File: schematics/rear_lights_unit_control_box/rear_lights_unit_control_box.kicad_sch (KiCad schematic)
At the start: 7 parts, among them J1 Conn_01x04_Pin, SW1 SW_SPDT, SW2 SW_SPDT

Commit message: more schematic updates
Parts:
- removed J1: Conn_01x04_Pin, symbol Connector:Conn_01x04_Pin
- added C1, C2: 0.1uF, symbol Device:C
- added C3: 10uF, symbol Device:C_Polarized
- added J1: Conn_01x04_Socket, symbol Connector:Conn_01x04_Socket
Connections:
- net GND: now also C1.1, C2.1, C3.2, J1.4 (Pin_4)
- net LEFT_TURN_EN: now also J1.2 (Pin_2)
- net RIGHT_TURN_EN: now also J1.1 (Pin_1)
- net V_BATT: now also C1.2, C2.2, C3.1, J1.3 (Pin_3)
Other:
- note added: "keep bypass caps as close as possible to inputs"
- note added: "right angle JST"
- note removed: "JST connector (female, right-angle)"
- moved on the sheet: D1, D2, R1, R2, SW1, SW2

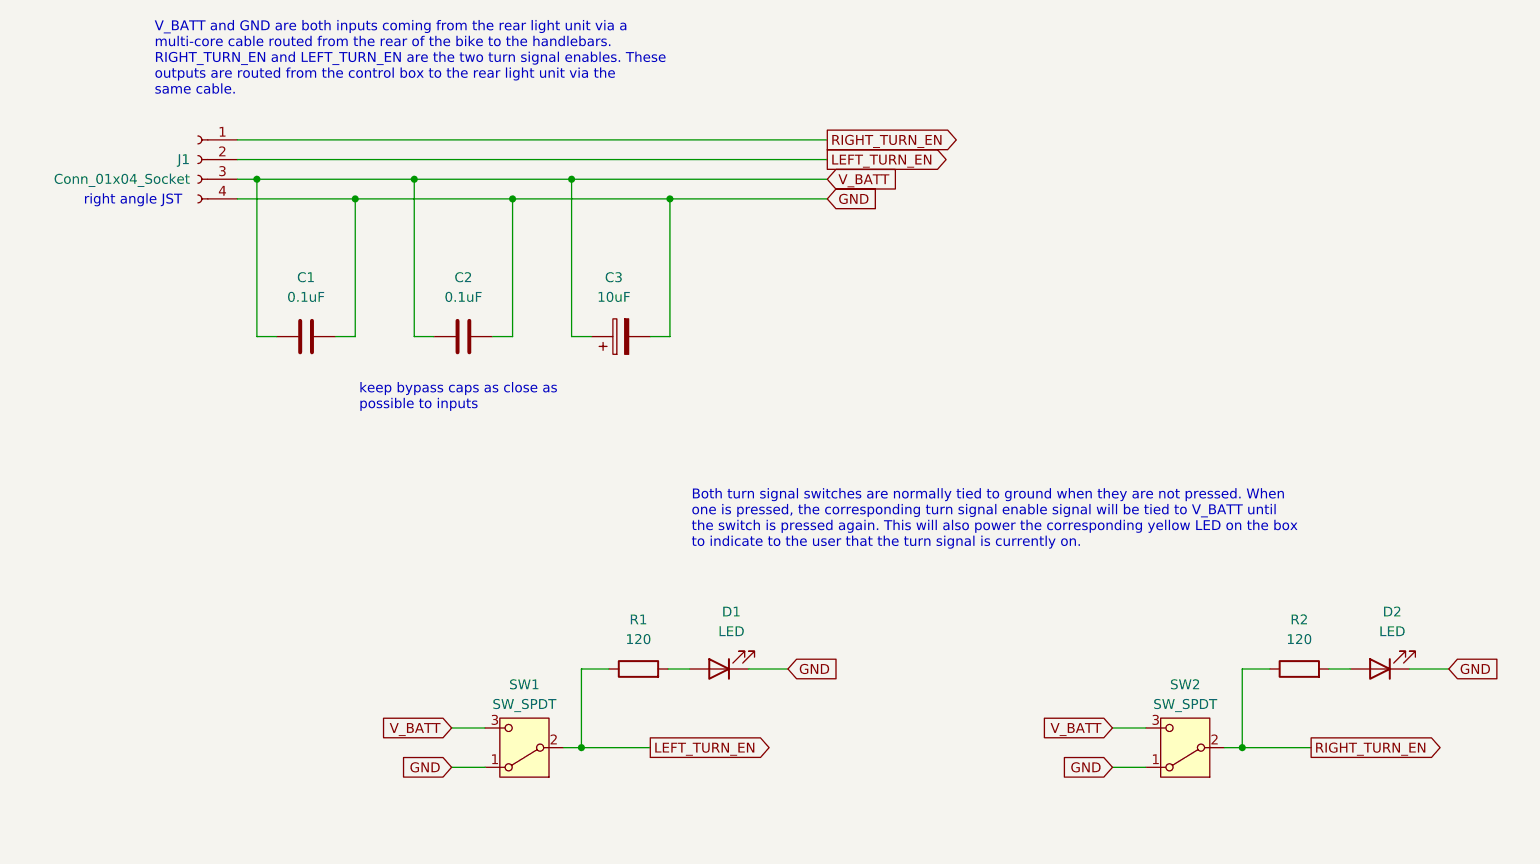
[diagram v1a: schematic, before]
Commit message: finalized rear light unit control box schematic, added corresponding BOM
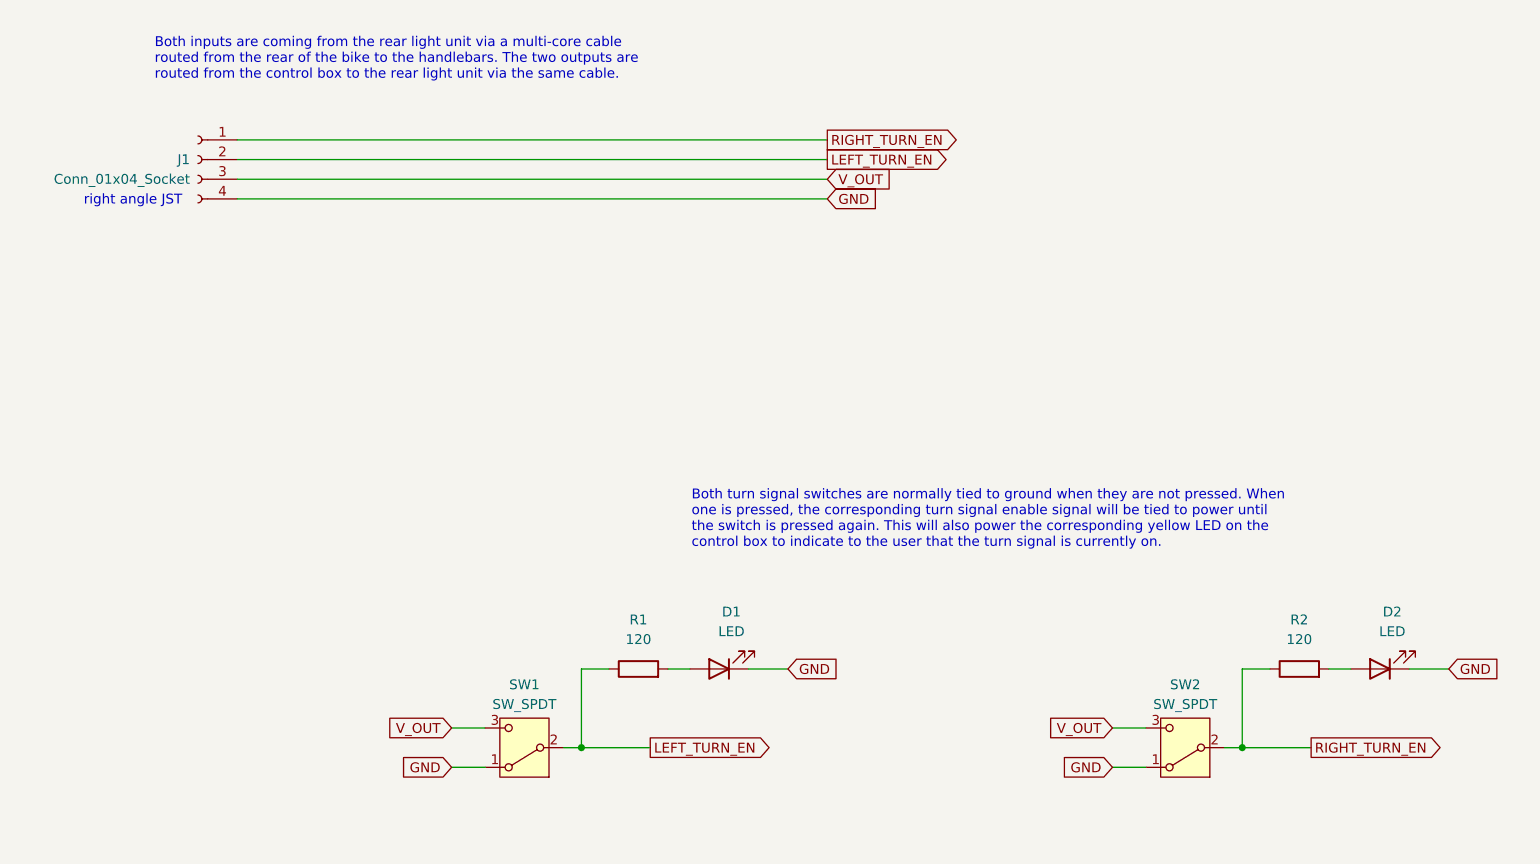
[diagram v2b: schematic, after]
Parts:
- removed C1, C2: 0.1uF, symbol Device:C
- removed C3: 10uF, symbol Device:C_Polarized
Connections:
- net V_BATT renamed V_OUT
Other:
- note added: "Both inputs are coming from the rear light unit via a multi-core cable routed from the rear of the bike to the handlebars. The two outputs are routed from the control box to the rear light unit via the same cable."
- note added: "Both turn signal switches are normally tied to ground when they are not pressed. When one is pressed, the corresponding turn signal enable signal will be tied to power until the switch is pressed again. This will also power the corresponding yellow LED on the control box to indicate to the user that the turn signal is currently on."
- note removed: "Both turn signal switches are normally tied to ground when they are not pressed. When one is pressed, the corresponding turn signal enable signal will be tied to V_BATT until the switch is pressed again. This will also power the corresponding yellow LED on the box to indicate to the user that the turn signal is currently on."
- note removed: "V_BATT and GND are both inputs coming from the rear light unit via a multi-core cable routed from the rear of the bike to the handlebars. RIGHT_TURN_EN and LEFT_TURN_EN are the two turn signal enables. These outputs are routed from the control box to the rear light unit via the same cable."
- note removed: "keep bypass caps as close as possible to inputs"

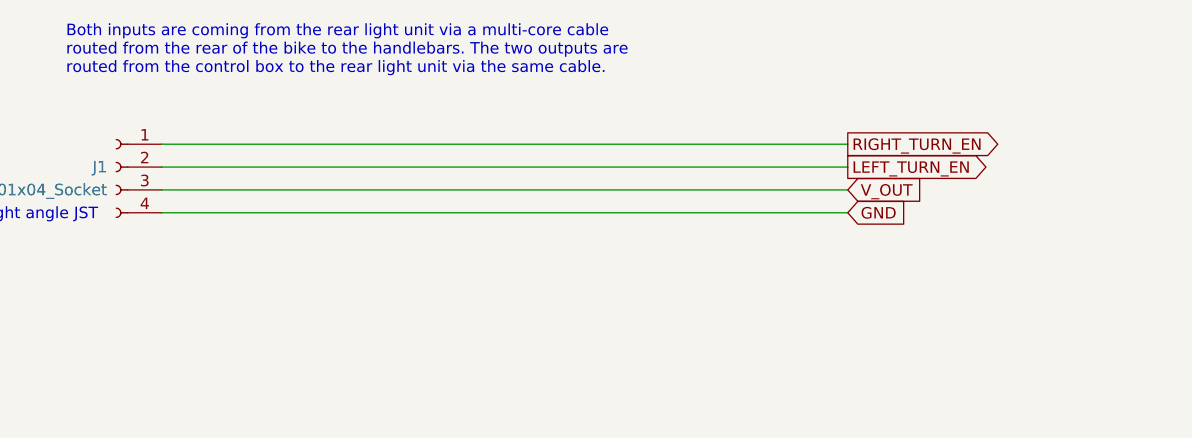
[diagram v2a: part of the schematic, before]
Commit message: rear light control box: added test points to I/O signals, improved BOM (added specific part numbers, descriptions, etc), started PCB layout. started project footprint file, fixed error in TP4056 symbol (had two pin 5's)
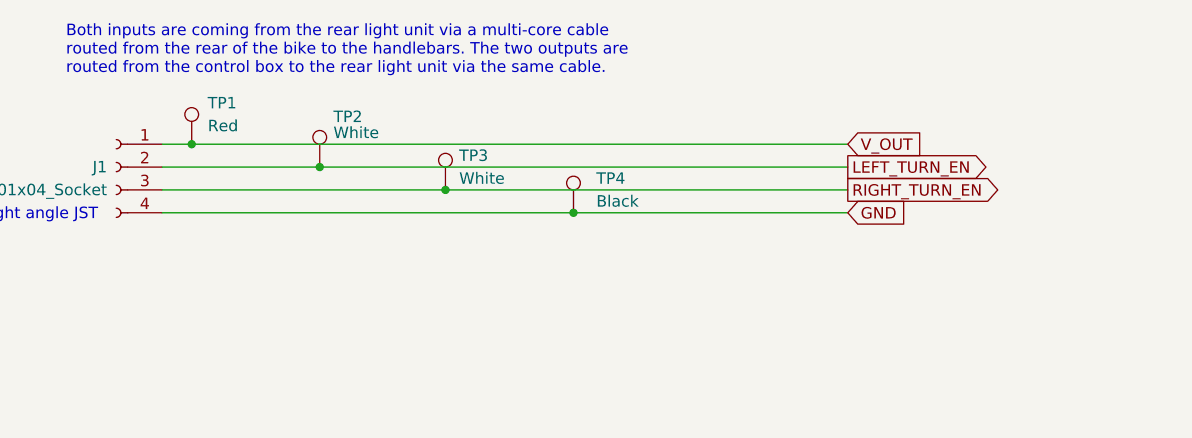
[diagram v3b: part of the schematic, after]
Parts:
- added TP1: Red, TestPoint:TestPoint_Keystone_5000-5004_Miniature, symbol Connector:TestPoint
- added TP2, TP3: White, TestPoint:TestPoint_Keystone_5000-5004_Miniature, symbol Connector:TestPoint
- added TP4: Black, TestPoint:TestPoint_Keystone_5000-5004_Miniature, symbol Connector:TestPoint
- D1, D2: footprint (none) -> LED_THT:LED_D5.0mm; Part Num (none) -> CHANZON yellow LED
- J1: footprint (none) -> Connector_JST:JST_XH_S4B-XH-A-1_1x04_P2.50mm_Horizontal; Part Num (none) -> JST XH-2.54
- R1, R2: footprint (none) -> Resistor_THT:R_Axial_DIN0207_L6.3mm_D2.5mm_P10.16mm_Horizontal; Part Num (none) -> MFR25SFTF52-120R
- SW1, SW2: footprint (none) -> Button_Switch_THT:SW_Push_2P2T_Toggle_CK_PVA2xxH2xxxxxxV2; Part Num (none) -> SPDT SW
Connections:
- net GND: now also TP4.1
- net LEFT_TURN_EN: now also TP2.1
- net RIGHT_TURN_EN: now also J1.3 (Pin_3), TP3.1; no longer J1.1 (Pin_1)
- net V_OUT: now also J1.1 (Pin_1), TP1.1; no longer J1.3 (Pin_3)

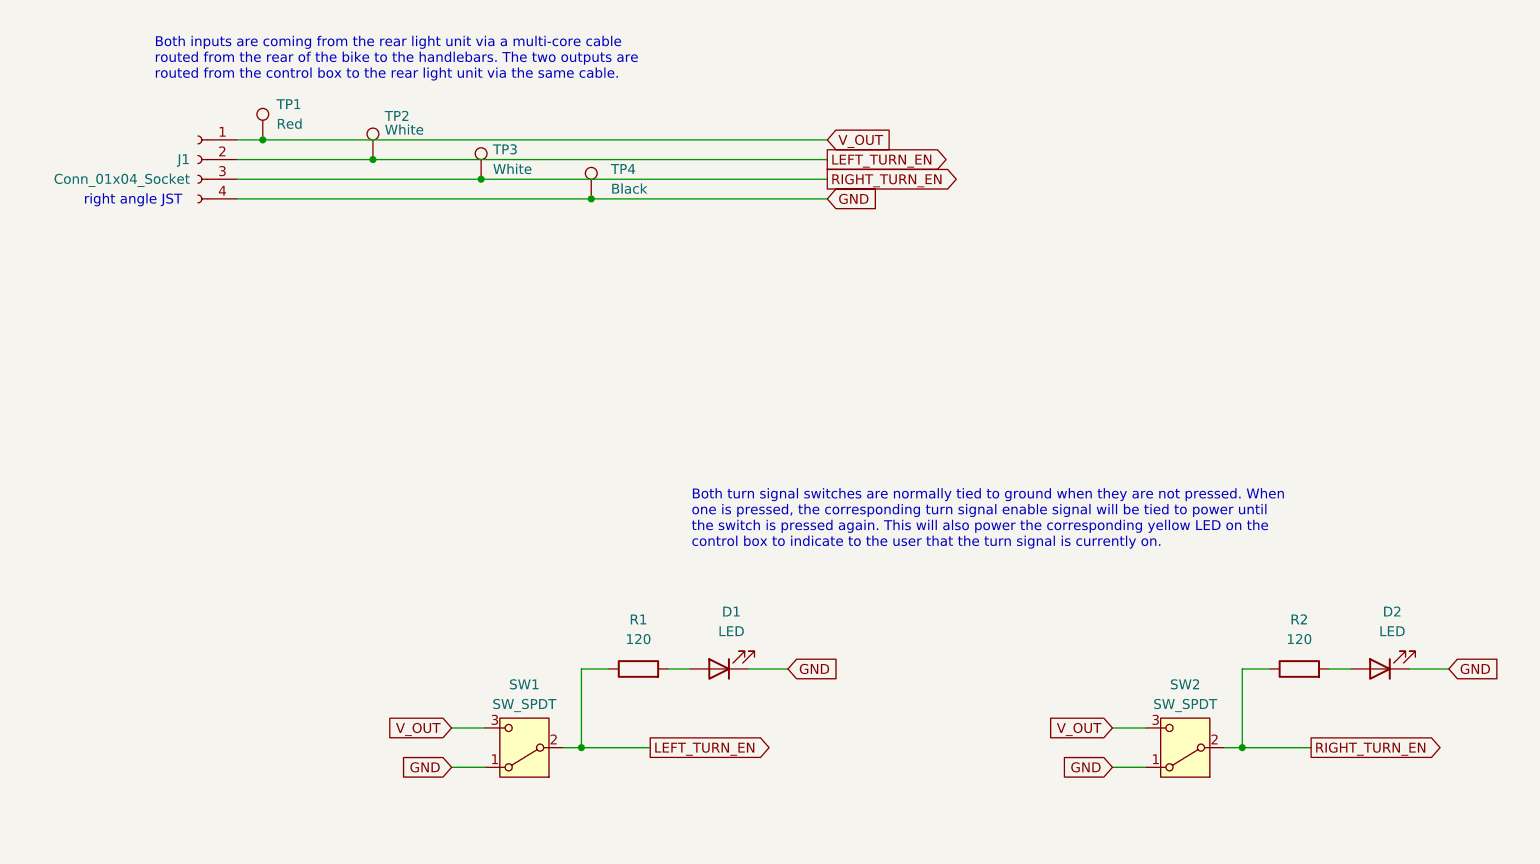
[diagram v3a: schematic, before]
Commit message: rear light unit control box: finished first draft of PCB
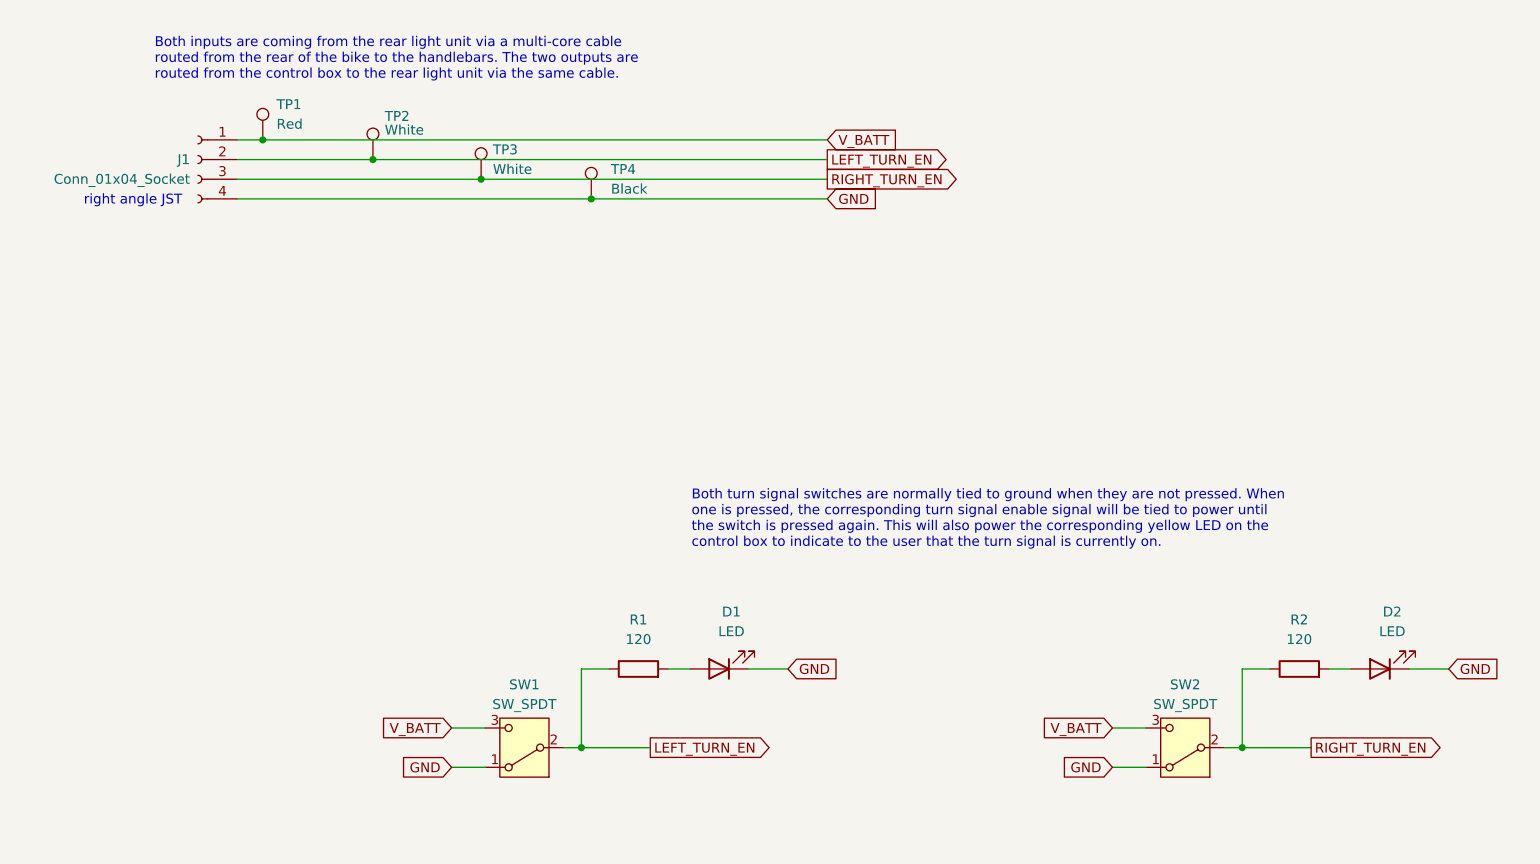
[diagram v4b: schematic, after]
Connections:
- net V_OUT renamed V_BATT
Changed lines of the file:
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@@
 		)
 	)
-	(global_label "V_OUT"
+	(global_label "V_BATT"
 		(shape input)
 		(at 137.16 40.64 0)
@@
 		)
 		(property "Intersheetrefs" "${INTERSHEET_REFS}"
-			(at 145.83 40.64 0)
+			(at 146.4952 40.64 0)
 			(effects
 				(font
@@
 		)
 	)
-	(global_label "V_OUT"
+	(global_label "V_BATT"
 		(shape input)
 		(at 173.99 116.586 180)
@@
 		)
 		(property "Intersheetrefs" "${INTERSHEET_REFS}"
-			(at 165.32 116.586 0)
+			(at 164.6548 116.586 0)
 			(effects
 				(font
@@
 		)
 	)
-	(global_label "V_OUT"
+	(global_label "V_BATT"
 		(shape input)
 		(at 88.646 116.586 180)
@@
 		)
 		(property "Intersheetrefs" "${INTERSHEET_REFS}"
-			(at 79.976 116.586 0)
+			(at 79.3108 116.586 0)
 			(effects
 				(font

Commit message: fixed page size for rear light control box PCB so I can print to scale, regenerated related files
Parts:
- R1, R2: Part Num MFR25SFTF52-120R -> MFR-25SFTF52-120R
- TP1: Part Num Keystone Electronics 5000 -> Keystone Electronics 5000
- TP2, TP3: Part Num Keystone Electronics 5001 -> Keystone Electronics 5001
- TP4: Part Num Keystone Electronics 5002 -> Keystone Electronics 5002
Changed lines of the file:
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@@
 			)
 		)
-		(property "Part Num" " Keystone Electronics 5000"
+		(property "Part Num" "Keystone Electronics 5000"
 			(at 64.262 40.64 0)
 			(effects
@@
 			)
 		)
-		(property "Part Num" " Keystone Electronics 5001"
+		(property "Part Num" "Keystone Electronics 5001"
 			(at 78.486 43.18 0)
 			(effects
@@
 			)
 		)
-		(property "Part Num" " Keystone Electronics 5002"
+		(property "Part Num" "Keystone Electronics 5002"
 			(at 106.68 48.26 0)
 			(effects
@@
 			)
 		)
-		(property "Description" "Resistor, 0.5 W, 1%"
+		(property "Description" "Resistor, 0.25 W, 1%"
 			(at 198.12 108.966 0)
 			(effects
@@
 			)
 		)
-		(property "Part Num" "MFR25SFTF52-120R"
+		(property "Part Num" "MFR-25SFTF52-120R  "
 			(at 198.12 108.966 90)
 			(effects
@@
 			)
 		)
-		(property "Part Num" " Keystone Electronics 5001"
+		(property "Part Num" "Keystone Electronics 5001"
 			(at 92.456 45.72 0)
 			(effects
@@
 			)
 		)
-		(property "Description" "Resistor, 0.5 W, 1%"
+		(property "Description" "Resistor, 0.25 W, 1%"
 			(at 112.776 108.966 0)
 			(effects
@@
 			)
 		)
-		(property "Part Num" "MFR25SFTF52-120R"
+		(property "Part Num" "MFR-25SFTF52-120R  "
 			(at 112.776 108.966 90)
 			(effects

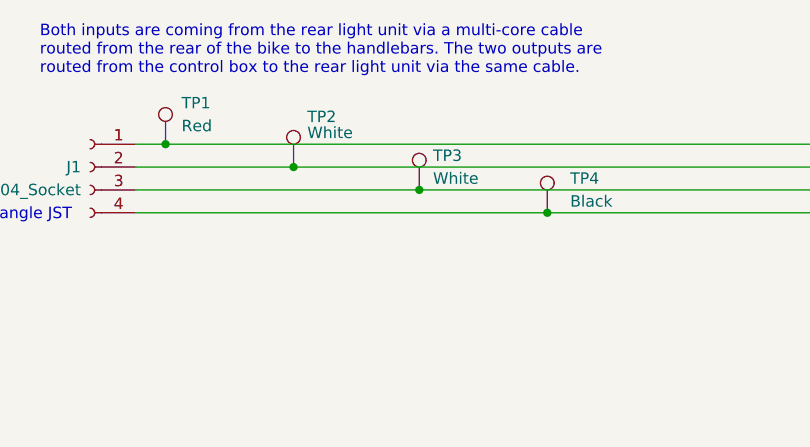
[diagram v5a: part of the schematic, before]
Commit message: more schematic updates: re-did bike computer with better ESP32 symbol, fixed component data on other schematics (somehow some of the part nums, descriptions, etc disappeared??)
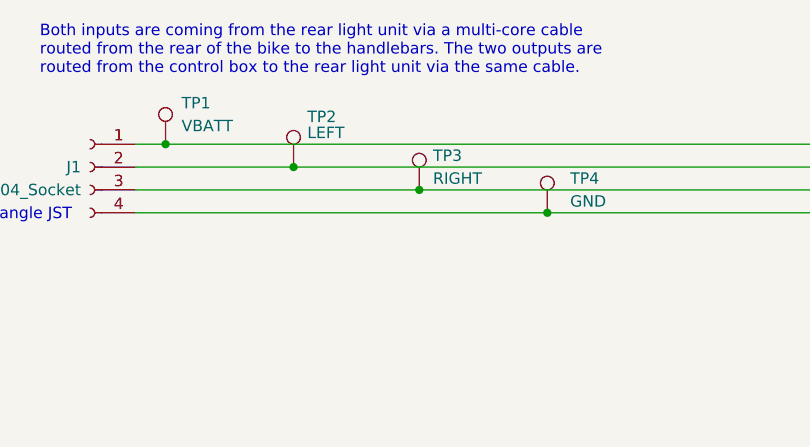
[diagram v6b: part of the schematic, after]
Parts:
- D1, D2: Part Num CHANZON yellow LED -> CHANZON 5mm LED
- TP1: value Red -> VBATT
- TP2: value White -> LEFT
- TP3: value White -> RIGHT
- TP4: value Black -> GND
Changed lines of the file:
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@@
 	(title_block
 		(title "FarrhadTech Rear Lights Unit Control Box")
-		(date "2025-03-26")
+		(date "2025-03-31")
 	)
 	(junction
@@
 			)
 		)
-		(property "Value" "Red"
+		(property "Value" "VBATT"
 			(at 66.04 38.6079 0)
 			(effects
@@
 			)
 		)
-		(property "Description" "Test point loop"
+		(property "Description" "Test point loop, red"
 			(at 64.262 40.64 0)
 			(effects
@@
 			)
 		)
-		(property "Value" "White"
+		(property "Value" "LEFT"
 			(at 80.01 39.37 0)
 			(effects
@@
 			)
 		)
-		(property "Description" "Test point loop"
+		(property "Description" "Test point loop, white"
 			(at 78.486 43.18 0)
 			(effects
@@
 			)
 		)
-		(property "Value" "Black"
+		(property "Value" "GND"
 			(at 109.22 46.99 0)
 			(effects
@@
 			)
 		)
-		(property "Description" "Test point loop"
+		(property "Description" "Test point loop, black"
 			(at 106.68 48.26 0)
 			(effects
@@
 			)
 		)
-		(property "Value" "White"
+		(property "Value" "RIGHT"
 			(at 93.98 44.45 0)
 			(effects
@@
 			)
 		)
-		(property "Description" "Test point loop"
+		(property "Description" "Test point loop, white"
 			(at 92.456 45.72 0)
 			(effects
@@
 			)
 		)
-		(property "Description" "Light emitting diode"
+		(property "Description" "Light emitting diode, yellow"
 			(at 123.19 108.966 0)
 			(effects
@@
 			)
 		)
-		(property "Part Num" "CHANZON yellow LED"
+		(property "Part Num" "CHANZON 5mm LED"
 			(at 123.19 108.966 0)
 			(effects
@@
 			)
 		)
-		(property "Description" "Light emitting diode"
+		(property "Description" "Light emitting diode, yellow"
 			(at 208.534 108.966 0)
 			(effects
@@
 			)
 		)
-		(property "Part Num" "CHANZON yellow LED"
+		(property "Part Num" "CHANZON 5mm LED"
 			(at 208.534 108.966 0)
 			(effects

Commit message: finalized rear light unit v0
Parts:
- SW1: symbol Switch:SW_SPDT -> FarrhadTech:SW_SPDT
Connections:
- net GND: now also SW1.3 (A); no longer SW1.1 (A)
- net V_BATT: now also SW1.1 (C); no longer SW1.3 (C)
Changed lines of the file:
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@@
 	)
 	(symbol
-		(lib_id "Switch:SW_SPDT")
+		(lib_id "FarrhadTech:SW_SPDT")
 		(at 98.044 119.126 180)
 		(unit 1)
@@
 		(fields_autoplaced yes)
 		(property "Reference" "SW1"
-			(at 98.044 110.998 0)
+			(at 98.044 110.49 0)
 			(effects
 				(font
@@
 		)
 		(property "Value" "SW_SPDT"
-			(at 98.044 113.538 0)
+			(at 98.044 113.03 0)
 			(effects
 				(font
